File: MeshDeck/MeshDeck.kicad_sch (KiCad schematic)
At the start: 32 parts, among them CN1 ATGM336H-6N-74, SW1 4*4*1.7, SW2 4*4*1.7, U1 ESP32-S3-WROOM-1U-N16R8, U2 SX1262S8S+T-X1, U5 RN32768114

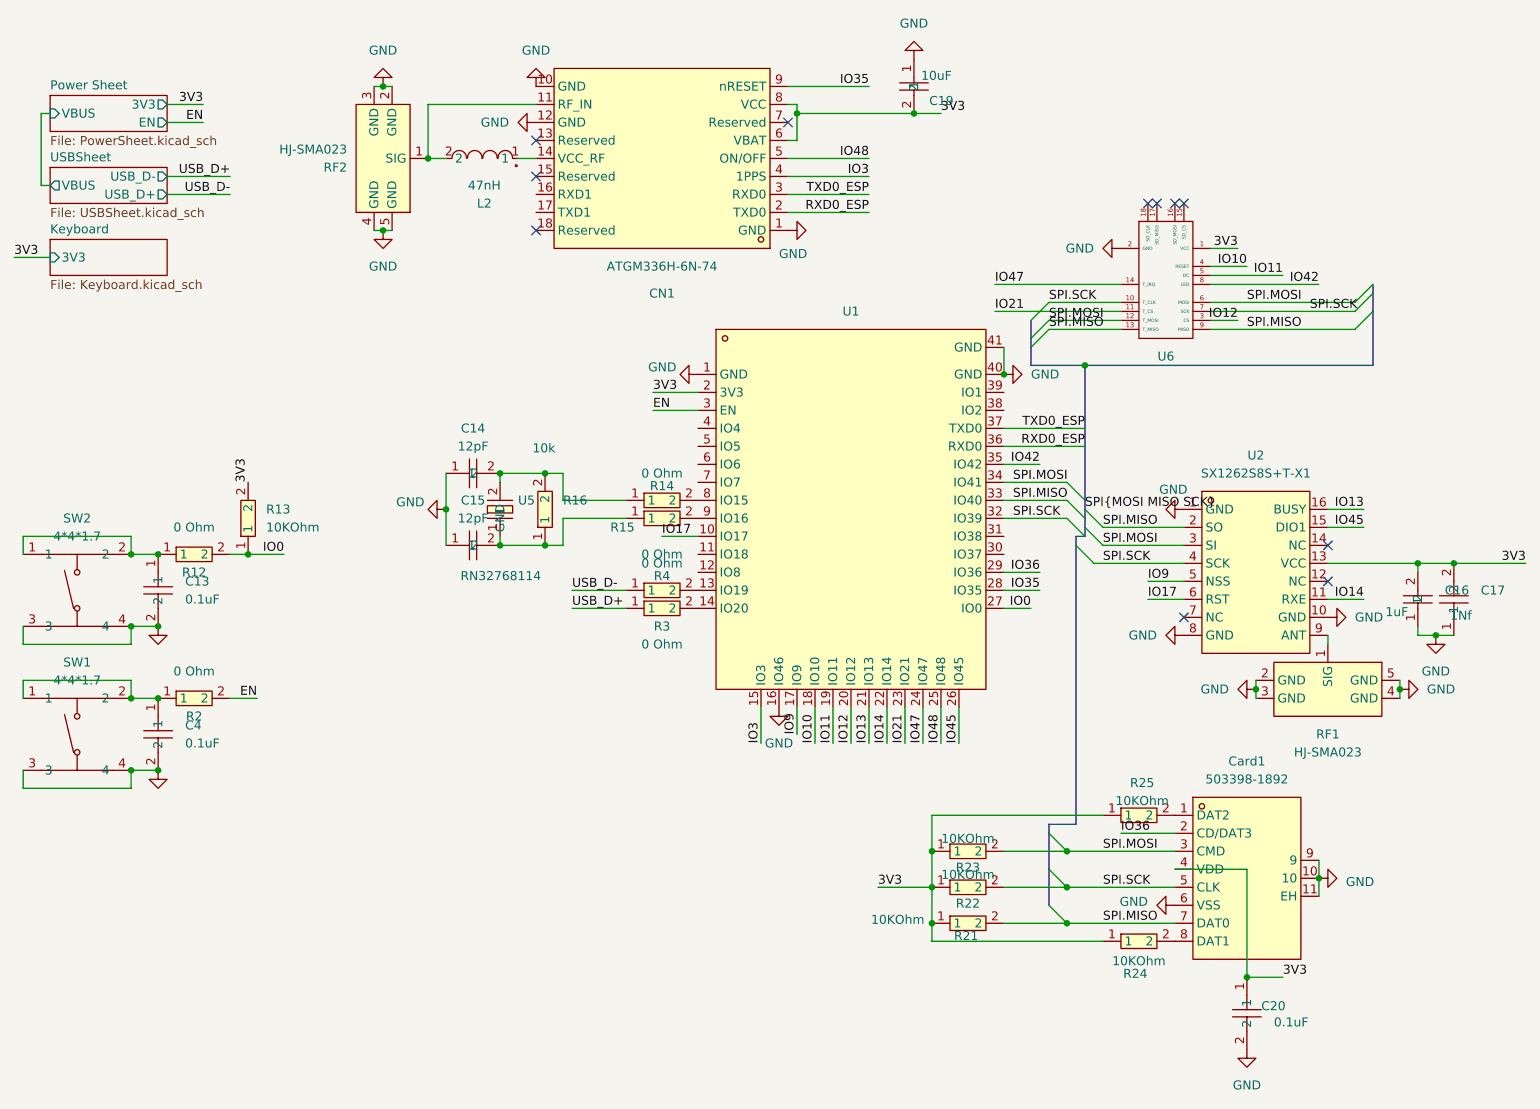
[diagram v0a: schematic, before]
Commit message: started pcb plus pin socket for expansion
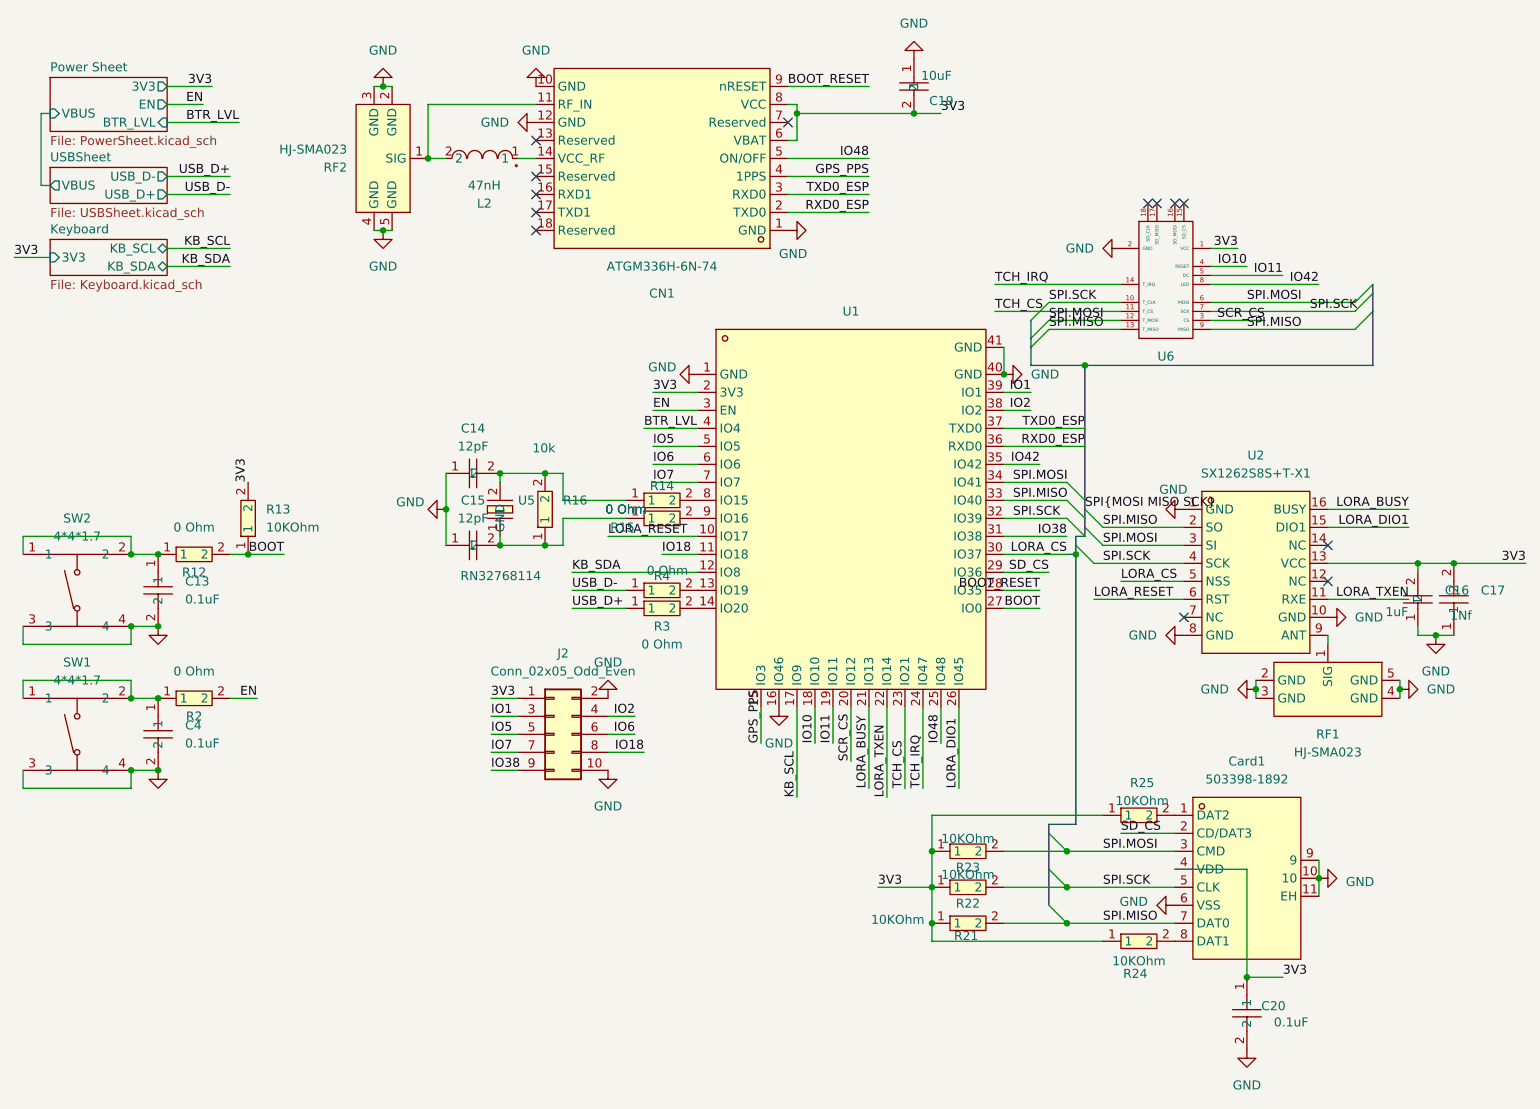
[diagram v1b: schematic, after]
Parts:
- added J2: Conn_02x05_Odd_Even, Connector_PinSocket_2.54mm:PinSocket_2x05_P2.54mm_Horizontal, symbol Connector_Generic:Conn_02x05_Odd_Even
- C17: LCSC Part C105226 -> C1523
- R13, R21, R22, R23, R24, R25: LCSC Part C176101 -> C25531
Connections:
- net 3V3: now also J2.1 (Pin_1)
- net GND: now also J2.10 (Pin_10), J2.2 (Pin_2)
- net IO18: now reaches U1.11 (IO18)
- net IO18: now also J2.8 (Pin_8)
- net KB_SDA: now reaches U1.12 (IO8)
- net LORA_CS: now reaches U1.30 (IO37)
- net LORA_CS: now also U2.5 (NSS)
- net IO38: now reaches U1.31 (IO38)
- net IO38: now also J2.9 (Pin_9)
- net IO2: now reaches U1.38 (IO2)
- net IO2: now also J2.4 (Pin_4)
- net IO1: now reaches U1.39 (IO1)
- net IO1: now also J2.3 (Pin_3)
- net BTR_LVL: now reaches U1.4 (IO4)
- net IO5: now reaches U1.5 (IO5)
- net IO5: now also J2.5 (Pin_5)
- net IO6: now reaches U1.6 (IO6)
- net IO6: now also J2.6 (Pin_6)
- net IO7: now reaches U1.7 (IO7)
- net IO7: now also J2.7 (Pin_7)
- net IO0 renamed BOOT
- net IO12 renamed SCR_CS
- net IO13 renamed LORA_BUSY
- net IO14 renamed LORA_TXEN
- net IO17 renamed LORA_RESET
- net IO21 renamed TCH_CS
- net IO3 renamed GPS_PPS
- net IO35 renamed BOOT_RESET
- net IO36 renamed SD_CS
- net IO45 renamed LORA_DIO1
- net IO47 renamed TCH_IRQ
- net IO9 renamed KB_SCL
- net KB_SCL: no longer U2.5 (NSS)
- no-connect marks 11 -> 13
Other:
- sheet Keyboard ports: added KB_SCL, KB_SDA; removed none
- sheet Power Sheet ports: added BTR_LVL; removed none

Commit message: Too much routing
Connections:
- net IO10 renamed SCR_RESET
- net IO11 renamed SCR_CD
- net IO42 renamed SCR_LED
- net IO48 renamed GPS_EN
